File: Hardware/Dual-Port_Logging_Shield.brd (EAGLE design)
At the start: 22.9 x 58.4 mm, 104 parts, among them IC1 USB224X_2241, J2 MICRO-SD-PUSH-PUSH-EXT-PIN, J3 AVR_SPI_PROG_3X2TESTPOINTS, J4 THING_PLUS, Q1 20V/4.2A/52mΩ/1.4W, Q2 20V/0.2A/8MHz/1.2Ω/1Vth, Q3 20V/4.2A/52mΩ/1.4W, Q4 20V/4.2A/52mΩ/1.4W, Q6 20V/4.2A/52mΩ/1.4W, U1 3.3V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

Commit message: Final Eagle files for Proto
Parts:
- removed U$14: (no value), output:DUAL#PORT_MICROSD_SHIELD0
- added D+, D-, MICROSD_VCC, V_USB: TEST-POINT3, SparkFun-Connectors:PAD.03X.03
- added D3: PRTR5V0U2F, SparkFun-IC-Power:SOT886
- added U$6: (no value), output:DUAL#PORT_LOGGING_SHIELD0
- moved GND 28.2 mm to (7.62, 3.81)
- moved FD1 21.6 mm to (0.64, 54.0)
- moved FD2 21.6 mm to (22.2, 4.45)
- moved FD3 21.6 mm to (22.2, 4.45)
- moved FD4 21.6 mm to (0.64, 54.0)
- moved R9 3.06 mm to (19.7, 6.35), turned to 180 degrees
- moved C5 0.52 mm to (19.7, 11.4)
- moved Q3 0.36 mm to (19.7, 8.89)
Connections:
- new net D+_IN: D+.1, D3.6, J1.A6, J1.B6
- new net D-_IN: D-.1, D3.4, J1.A7, J1.B7
- net D+: now also D3.1; no longer J1.A6, J1.B6
- net D-: now also D3.3; no longer J1.A7, J1.B7
- net GND: now also D3.2
- net MICROSD_VCC: now also MICROSD_VCC.1
- net V_USB: now also D3.5, V_USB.1
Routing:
- net D-_IN: track 0.00 -> 19.6 mm, vias 0 -> 2
- net D+_IN: track 0.00 -> 19.2 mm, vias 0 -> 2
- net V_USB: track 57.4 -> 66.6 mm, vias 0 -> 1
- net D-: track 47.3 -> 39.5 mm
- net D+: track 44.1 -> 37.1 mm
- net GND: track 42.2 -> 40.5 mm, vias 69 -> 75
- net MICROSD_VCC: track 11.6 -> 12.9 mm, vias 0 -> 1
- net MICROSD_PWR_EN: track 60.0 -> 59.0 mm
- net SDIO_VDD: track 36.8 -> 37.5 mm
- net VCC: track 29.0 -> 29.4 mm, vias 11 -> 12
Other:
- board text added: "1"
- board text added: "2"
- board text added: "3"
- board text added: "4"

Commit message: Updates post proto review
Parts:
- added R26, R27, R28: 100, SparkFun-Resistors:0402-TIGHT
- added U$14: (no value), output:DUAL#PORT_LOGGING_SHIELD0
- added U$18: (no value), output:#A4__#CS##6
- added U$19: (no value), output:#A3__#CS##6
- U$10: device output:#TXD#0 -> output:#TXD#1
- U$17: device output:##CS##0 -> output:#A5__#CS##0
- U$2: device output:#SCL#0 -> output:#SCL#1
- U$4: device output:#PICO#0 -> output:#PICO#1
- U$5: device output:#SCK#0 -> output:#SCK#2
- U$8: device output:#3V3#0 -> output:#3V3#1
- moved LOGO2 6.38 mm to (19.1, 38.1), turned to 90 degrees
- moved U$17 3.68 mm to (18.2, 36.8)
- moved C8 3.24 mm to (18.4, 23.5)
- moved U$10 3.05 mm to (18.3, 47.0)
- moved U$9 3.05 mm to (18.3, 49.5)
- moved SD_WP 2.29 mm to (15.9, 35.6)
- moved U$3 2.29 mm to (20.7, 44.5)
- moved U$4 2.29 mm to (20.7, 41.9)
- moved R20 2.03 mm to (3.94, 34.5)
- moved U$1 2.03 mm to (2.16, 52.1)
- moved U$5 1.91 mm to (20.7, 39.4)
- moved U$7 1.91 mm to (20.7, 21.6)
- moved U$8 1.91 mm to (20.7, 16.5)
- moved U$2 1.91 mm to (2.16, 49.5)
- moved LOGO4 1.45 mm to (17.8, 51.4), turned to 90 degrees
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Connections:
- net AT_CIPO renamed AT_POCI
- new net N$6: Q3.1, R26.2, R9.1
- new net N$7: Q2.1, R20.2, R27.1
- new net N$8: Q2.3, R28.1
- net MICROSD_PWR_EN: now also R26.1; no longer Q3.1, R9.1
- net N$17: now also R28.2; no longer Q2.3
- net SDIO_EN: now also R27.2; no longer Q2.1, R20.2
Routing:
- net GND: track 40.5 -> 44.1 mm
- net MICROSD_PWR_EN: track 59.0 -> 62.0 mm
- net N$6: track 0.00 -> 2.69 mm
- net SD_!CD!: track 17.8 -> 20.4 mm
- net N$7: track 0.00 -> 2.51 mm
- net N$8: track 0.00 -> 1.80 mm
- net VCC: track 29.4 -> 31.1 mm
- net MICROSD_VCC: track 12.9 -> 11.5 mm
- net ACTIVITY: track 21.4 -> 22.7 mm
- net N$17: track 6.07 -> 7.09 mm
- net SDA: track 22.9 -> 22.1 mm
- net SD_WP: track 3.09 -> 2.33 mm
- net GPIO7: track 14.2 -> 13.6 mm
- net SD_D2: track 15.2 -> 15.8 mm
- net SDIO_VDD: track 37.5 -> 38.0 mm
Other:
- board text added: "4-Layer Board 1.6mm Thickness 1oz Copper (Outer layers) LeadFree HASL Finish"
- board text added: "v01"
- board text removed: "4-Layer Board 1.6mm Thickness 1oz Copper (Outer layers) HASL Finish"
- board text removed: "v10"

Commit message: Nudged the silk labels
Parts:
- moved U$1 0.51 mm to (1.65, 52.1)
- moved U$2 0.51 mm to (1.65, 49.5)
- moved U$3 0.38 mm to (21.1, 44.5)
- moved U$4 0.38 mm to (21.1, 41.9)
- moved U$5 0.38 mm to (21.1, 39.4)
- moved U$7 0.38 mm to (21.1, 21.6)
- moved U$8 0.38 mm to (21.1, 16.5)
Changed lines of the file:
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@@
 <element name="U$6" library="output" package="DUAL#PORT_LOGGING_SHIELD0" value="" x="11.43" y="8.89" smashed="yes" rot="MR0"/>
 <element name="U$14" library="output" package="DUAL#PORT_LOGGING_SHIELD0" value="" x="19.304" y="22.86" smashed="yes" rot="R90"/>
-<element name="U$1" library="output" package="#SDA#0" value="" x="2.159" y="52.07" smashed="yes" rot="MR0"/>
-<element name="U$2" library="output" package="#SCL#1" value="" x="2.159" y="49.53" smashed="yes" rot="MR0"/>
+<element name="U$1" library="output" package="#SDA#0" value="" x="1.651" y="52.07" smashed="yes" rot="MR0"/>
+<element name="U$2" library="output" package="#SCL#1" value="" x="1.651" y="49.53" smashed="yes" rot="MR0"/>
 <element name="U$9" library="output" package="#RXD#0" value="" x="18.288" y="49.53" smashed="yes" rot="MR0"/>
 <element name="U$10" library="output" package="#TXD#1" value="" x="18.288" y="46.99" smashed="yes" rot="MR0"/>
-<element name="U$3" library="output" package="#POCI#0" value="" x="20.701" y="44.45" smashed="yes" rot="MR0"/>
-<element name="U$4" library="output" package="#PICO#1" value="" x="20.701" y="41.91" smashed="yes" rot="MR0"/>
-<element name="U$5" library="output" package="#SCK#2" value="" x="20.701" y="39.37" smashed="yes" rot="MR0"/>
+<element name="U$3" library="output" package="#POCI#0" value="" x="21.082" y="44.45" smashed="yes" rot="MR0"/>
+<element name="U$4" library="output" package="#PICO#1" value="" x="21.082" y="41.91" smashed="yes" rot="MR0"/>
+<element name="U$5" library="output" package="#SCK#2" value="" x="21.082" y="39.37" smashed="yes" rot="MR0"/>
 <element name="U$17" library="output" package="#A5__#CS##0" value="" x="18.161" y="36.83" smashed="yes" rot="MR0"/>
 <element name="U$18" library="output" package="#A4__#CS##6" value="" x="18.288" y="34.29" smashed="yes" rot="MR0"/>
 <element name="U$19" library="output" package="#A3__#CS##6" value="" x="18.288" y="31.75" smashed="yes" rot="MR0"/>
-<element name="U$7" library="output" package="#GND#0" value="" x="20.701" y="21.59" smashed="yes" rot="MR0"/>
-<element name="U$8" library="output" package="#3V3#1" value="" x="20.701" y="16.51" smashed="yes" rot="MR0"/>
+<element name="U$7" library="output" package="#GND#0" value="" x="21.082" y="21.59" smashed="yes" rot="MR0"/>
+<element name="U$8" library="output" package="#3V3#1" value="" x="21.082" y="16.51" smashed="yes" rot="MR0"/>
 <element name="R26" library="SparkFun-Resistors" package="0402-TIGHT" value="100" x="19.685" y="6.223" smashed="yes">
 <attribute name="NAME" x="19.685" y="6.785" size="0.6096" layer="25" font="vector" ratio="20" align="bottom-center"/>

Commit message: Add v10 hardware files
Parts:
- removed SD_WP: TEST-POINT3, SparkFun-Connectors:PAD.03X.03
- added R29, R30: 10k, SparkFun-Resistors:0402-TIGHT
- added SH: JUMPER-SMT_2_NC_TRACE_SILK, SparkFun-Jumpers:SMT-JUMPER_2_NC_TRACE_SILK
- added U$20: (no value), output:#SH#0
- added U$21: (no value), output:G0
- added U$22: (no value), output:V0
- added U$23: (no value), output:D#0
- added U$25: (no value), output:D#1
- D+, D-, GND, V_USB: value TEST-POINT3 -> TEST-POINT3X5; device SparkFun-Connectors:PAD.03X.03 -> SparkFun-Connectors:PAD.03X.05
- IC1: value USB224X_2241 -> USB224X_2241_V04; device USB224x:36-QFN -> SparkFun-IC-Special-Function:36-QFN
- R21, R23: value 10k -> 100k
- R22, R24: value 47k -> 1M
- U2, U4, U5: device 74HC4066:14-QFN -> SparkFun-IC-Logic:14-QFN
- moved R25 0.45 mm to (16.8, 34.0), turned to 270 degrees
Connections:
- removed net SD_WP: IC1.30, SD_WP.1
- new net N$12: J1.SHLD1, J1.SHLD2, J1.SHLD3, J1.SHLD4, SH.1
- new net N$20: IC1.30, R29.1
- net 3.3V: now also R30.1
- net GND: now also R29.2, SH.2
- net POCI: now also R30.2
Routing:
- net N$12: track 0.00 -> 17.2 mm
- net N$20: track 0.00 -> 4.33 mm
- net POCI: track 20.3 -> 23.2 mm
- net GND: track 44.1 -> 46.6 mm, vias 75 -> 77
- net SD_WP: track 2.33 -> 0.00 mm, vias 1 -> 0
- net 3.3V: track 40.0 -> 41.4 mm
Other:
- board text added: "v10"
- board text removed: "v01"

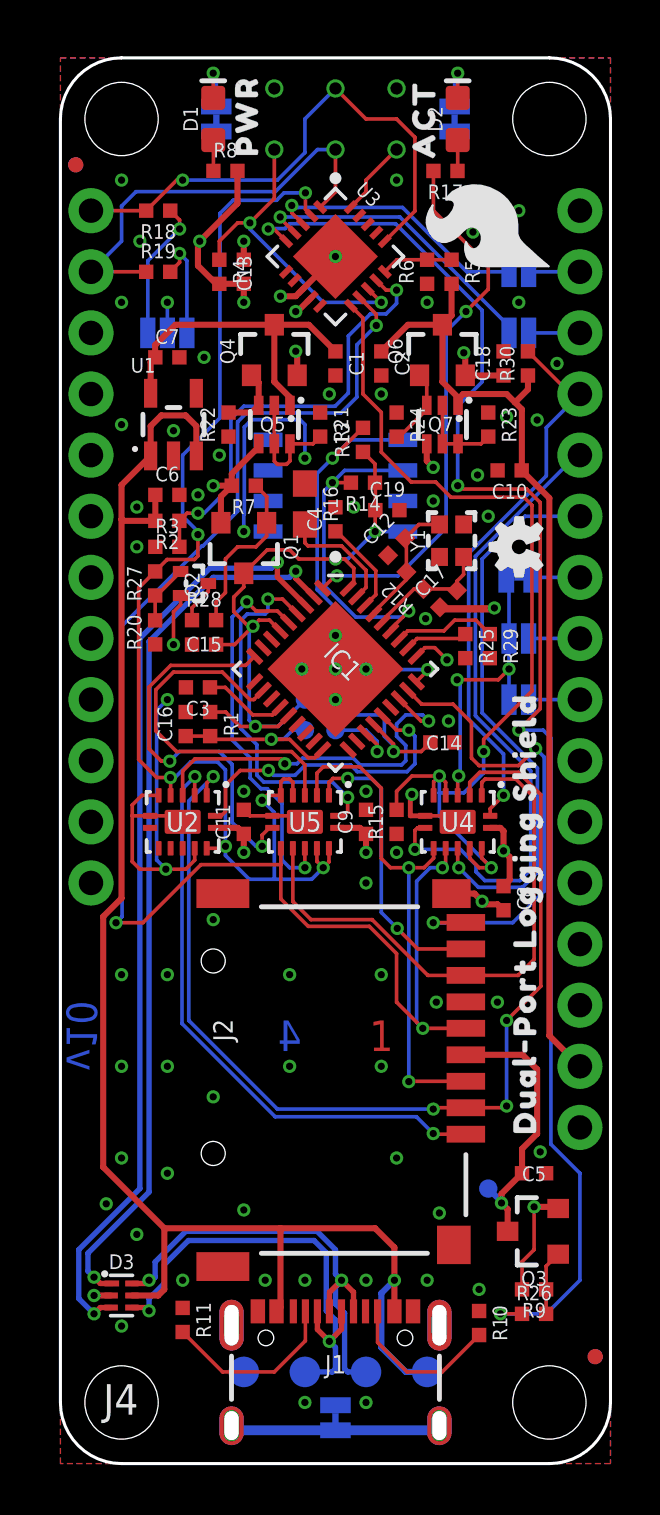
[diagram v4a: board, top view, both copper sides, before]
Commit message: Updated hardware files after REDS Review
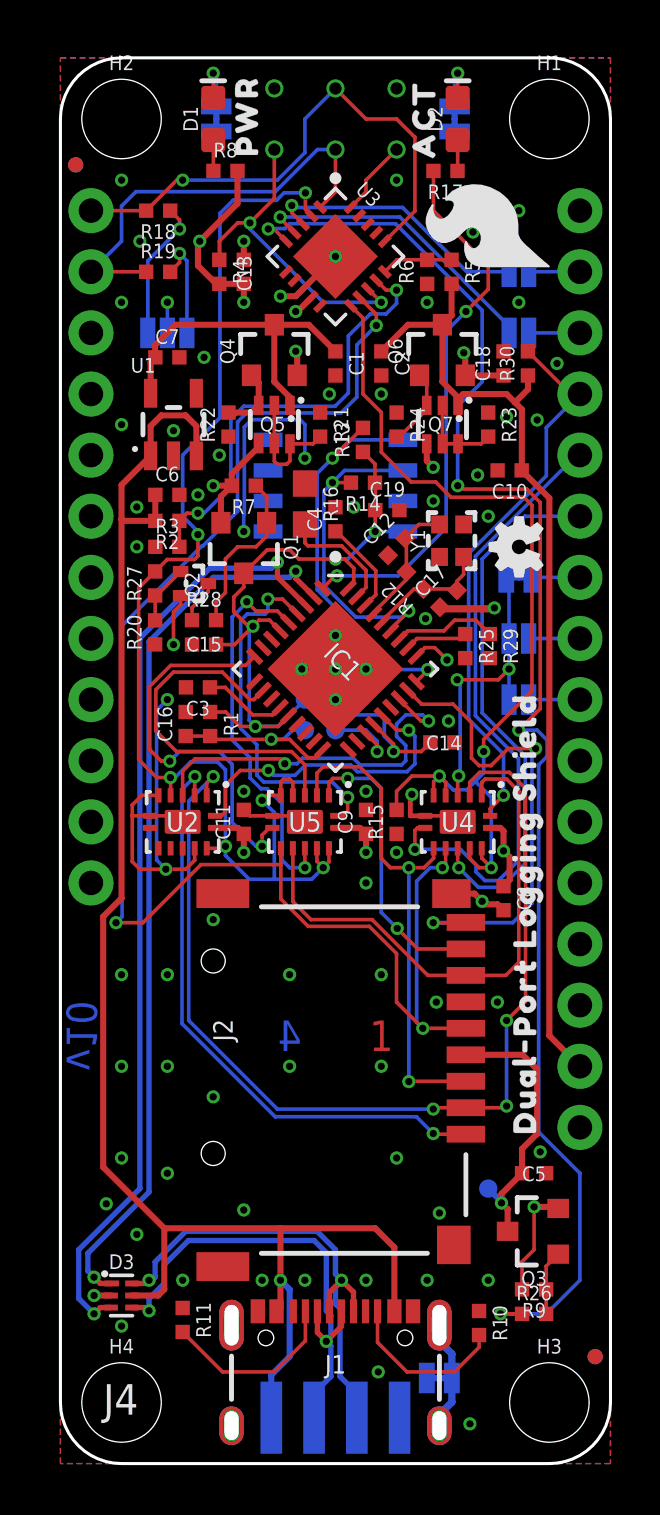
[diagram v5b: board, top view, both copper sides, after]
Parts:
- removed D+, D-, GND, V_USB: TEST-POINT3X5, SparkFun-Connectors:PAD.03X.05
- added H1, H2, H3, H4: STAND-OFF, SparkFun-Hardware:STAND-OFF
- added JP4: USB_SOLDER_PADS, SparkFun-Connectors:USB-SOLDER-PADS
- J4: device Thing_Plus:THING_PLUS -> SparkFun-Boards:THING_PLUS
- SH: value JUMPER-SMT_2_NC_TRACE_SILK -> JUMPER-SMT_2_NC_TRACE_NO-SILK; device SparkFun-Jumpers:SMT-JUMPER_2_NC_TRACE_SILK -> SparkFun-Jumpers:SMT-JUMPER_2_NC_TRACE_NO-SILK
- U$20: device output:#SH#0 -> output:SH0
- moved U$20 8.20 mm to (17.3, 3.56), turned to 90 degrees
- moved U$22 7.76 mm to (8.76, 4.32), turned to 90 degrees
- moved U$21 7.76 mm to (14.1, 4.19), turned to 90 degrees
- moved SH 4.62 mm to (15.7, 3.56), turned to 0 degrees
- moved U$23 0.64 mm to (10.5, 4.57), turned to 90 degrees
- moved U$25 0.59 mm to (12.3, 4.64), turned to 90 degrees
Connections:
- net D+_IN: now also JP4.D+; no longer D+.1
- net D-_IN: now also JP4.D-; no longer D-.1
- net GND: now also JP4.GND; no longer GND.1
- net V_USB: now also JP4.VBUS; no longer V_USB.1
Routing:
- net N$12: track 17.2 -> 21.6 mm
- net D+_IN: track 19.3 -> 20.6 mm
- net MICROSD_D0/SDO: track 23.6 -> 22.6 mm
- net PICO: track 27.0 -> 26.1 mm
- net SCLK: track 23.5 -> 22.5 mm
- net D-_IN: track 19.7 -> 20.6 mm
- net V_USB: track 66.6 -> 67.5 mm
- net MICROSD_D3/!CS!: track 43.8 -> 43.1 mm
- net SPI_EN: track 39.7 -> 39.0 mm

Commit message: PCB v1.1
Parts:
- added C20, C21, C22, C23, C24: 10uF, SparkFun-Capacitors:0402-TIGHT
- I2C: value JUMPER-SMT_3_NO_SILK -> JUMPER-SMT_3_2-NC_TRACE_SILK; device SparkFun-Jumpers:SMT-JUMPER_3_NO_SILK -> SparkFun-Jumpers:SMT-JUMPER_3_2-NC_TRACE_SILK
- moved R4 1.65 mm to (4.95, 49.5)
- moved C13 1.40 mm to (6.22, 49.5)
- moved C5 0.97 mm to (19.2, 12.9)
- moved C14 0.51 mm to (15.9, 30.5)
- moved R19 0.38 mm to (3.68, 49.5), turned to 270 degrees
- moved R7 0.38 mm to (7.62, 40.3)
- moved U$13 0.13 mm to (7.49, 47.0)
- moved Q3 0.13 mm to (19.7, 9.53)
- moved R26 0.06 mm to (19.7, 6.16)
- moved R9 0.06 mm to (19.7, 7.18)
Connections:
- net GND: now also C20.2, C21.2, C22.2, C23.2, C24.2
- net VCC: now also C20.1, C21.1, C22.1, C23.1, C24.1
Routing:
- net VCC: track 31.1 -> 40.6 mm, vias 12 -> 16
- net GND: track 46.6 -> 55.1 mm, vias 77 -> 79
- net MICROSD_PWR_EN: track 62.1 -> 60.5 mm
- net !RESET!: track 13.6 -> 15.0 mm
- net SD_D2: track 15.8 -> 14.6 mm
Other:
- board text added: "v11"
- board text removed: "v10"
